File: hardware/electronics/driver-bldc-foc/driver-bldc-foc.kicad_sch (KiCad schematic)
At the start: 2 parts, among them U3 AP1117-33, U4 TPS563240

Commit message: fix pcb 20.7.1635
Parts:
- removed U4: TPS563240, symbol Custom:TPS563240
- added C10, C11, C6, C8: 100nF, Capacitor_SMD:C_0805_2012Metric, symbol JLCPCB-Capacitors:0805,10uF
- added C12, C5: 10uF, Capacitor_SMD:C_0805_2012Metric, symbol JLCPCB-Capacitors:0805,10uF
- added C7, C9: 1uF, Capacitor_SMD:C_0805_2012Metric, symbol JLCPCB-Capacitors:0805,10uF
- added D1, D2: PMEG4005CEJ, Diode_SMD:D_SOD-323F, symbol Diode:PMEG4005CEJ
- added J1: VBUS, Connector_Wire:SolderWirePad_1x01_SMD_5x10mm, symbol Connector_Generic:Conn_01x01
- added J2: GND, Connector_Wire:SolderWirePad_1x01_SMD_5x10mm, symbol Connector_Generic:Conn_01x01
- added J3: USB_A, Connector_USB:USB_B_OST_USB-B1HSxx_Horizontal, symbol Connector:USB_A
- added J4: Motor_Phase_A, Connector_Wire:SolderWirePad_1x01_SMD_5x10mm, symbol Connector_Generic:Conn_01x01
- added J5: Motor_Phase_B, Connector_Wire:SolderWirePad_1x01_SMD_5x10mm, symbol Connector_Generic:Conn_01x01
- added J6: Motor_Phase_C, Connector_Wire:SolderWirePad_1x01_SMD_5x10mm, symbol Connector_Generic:Conn_01x01
- added L3: 1.5uH, Inductor_SMD:L_APV_ANR5040, symbol Device:L_Ferrite_Small
- added R3, R5, R6: 3k, Resistor_SMD:R_0805_2012Metric, symbol Device:R_Small
- added R4: 22k, Resistor_SMD:R_0805_2012Metric, symbol Device:R_Small
- added U1: TPS563240DDC, Package_TO_SOT_SMD:SOT-23-6, symbol Regulator_Switching:TPS563240DDC
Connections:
- net GND: now reaches U3.1 (GND)
- net GND: now also C10.2, C12.2, C5.2, C6.2, C7.2, C8.2, C9.2, J2.1 (Pin_1), R3.2, R6.2, U1.1 (GND)
- net +3.3V: now reaches U3.2 (VO)
- net +3.3V: now also C7.1, C8.1
- net +5V: now reaches U3.3 (VI)
- net +5V: now also C5.1, C6.1, D1.1 (K), D2.1 (K)
- new net: R3.1, R4.1, U1.4 (VFB)
- new net: C11.2, L3.1, U1.2 (SW)
- new net: C11.1, U1.6 (VBST)
- new net +12V: C10.1, C9.1, U1.3 (VIN), U1.5 (EN)
- new net 5V_BUCK: D2.2 (A), L3.2, R4.2
- new net USB_VBUS: D1.2 (A)
- new net VBUS: J1.1 (Pin_1), R5.1
- new net VbusSense: C12.1, R5.2, R6.1
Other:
- moved on the sheet: U3

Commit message: update main schematic
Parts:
- C12: value 10uF -> 1nF
- R5: value 3k -> 100k
- R6: value 3k -> 3.9k
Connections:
- net ThreePhaseBridge and Power/PHASE_C: now reaches J6.1 (Pin_1)
- net ThreePhaseBridge and Power/PHASE_A: now reaches J4.1 (Pin_1)
- net ThreePhaseBridge and Power/PHASE_B: now reaches J5.1 (Pin_1)
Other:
- sheet MCU ports: added 3V3_IN, DRV_EN, DRV_MISO, DRV_MOSI, DRV_SCK, DVR_CS, GND_IN, IA, IB, IC, OC, PWM_A+, PWM_A-, PWM_B+, PWM_B-, PWM_C+, PWM_C-, USB_D+, USB_D-, VA, VB, VBUS_SENSE, VC; removed none
- sheet ThreePhaseBridge and Power ports: added 3V3_IN, CUR_A, CUR_B, CUR_C, EN, FAULT, GND, INHA, INHB, INHC, INLA, INLB, INLC, PHASE_A, PHASE_B, PHASE_C, SPI_CLK, SPI_CS, SPI_MISO, SPI_MOSI, VBUS, VSENS_A, VSENS_B, VSENS_C; removed none

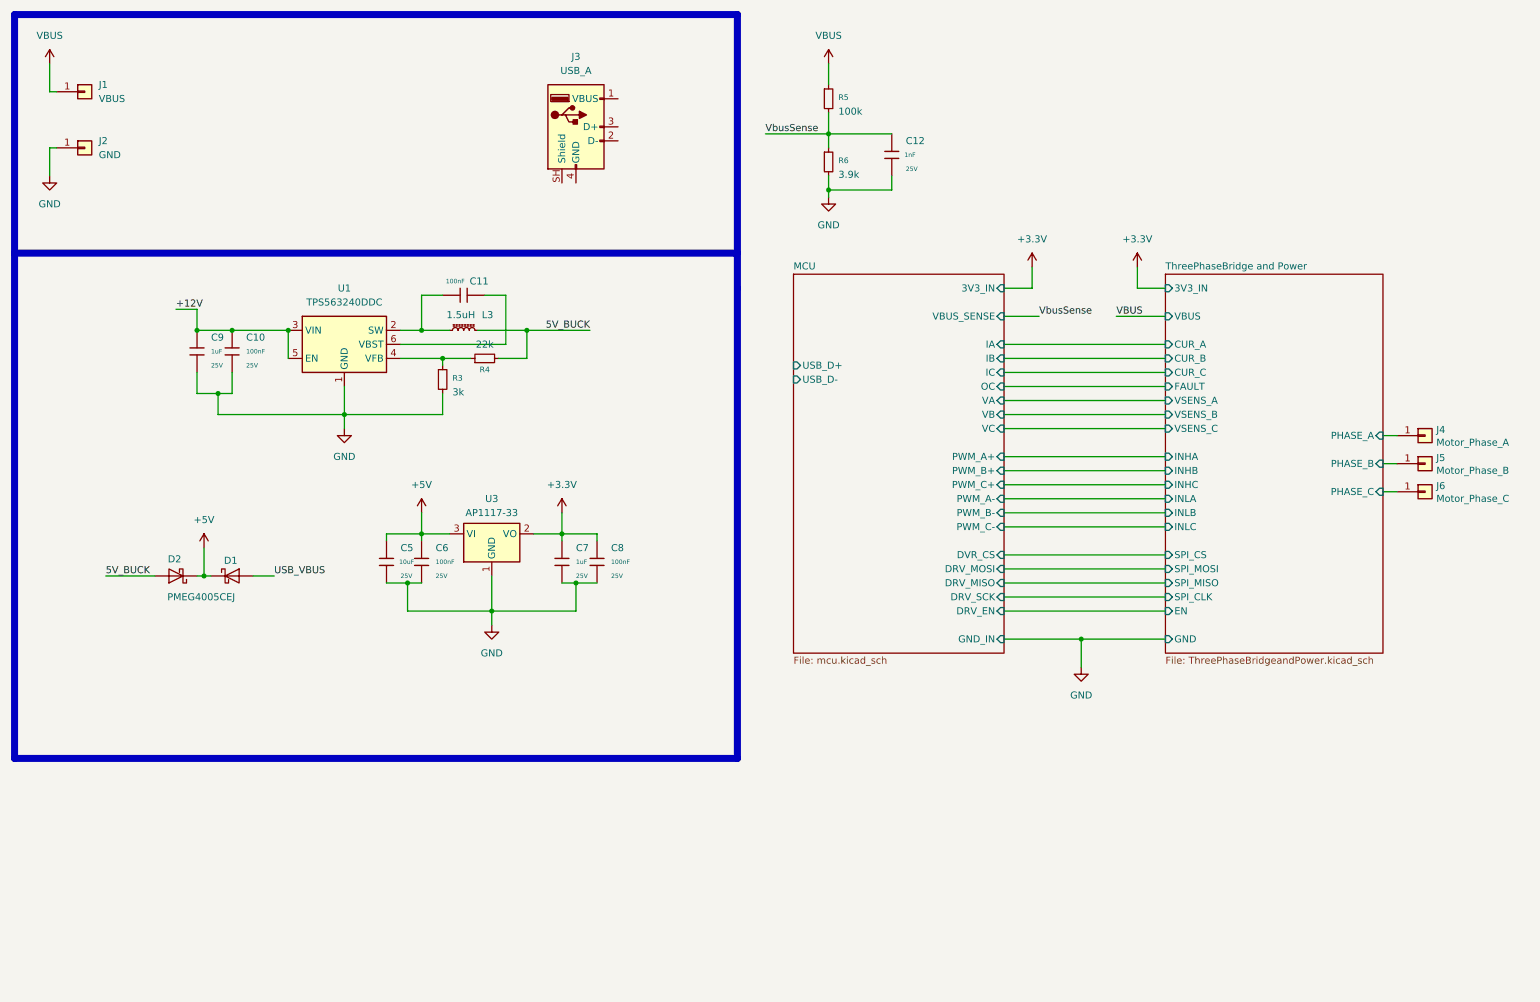
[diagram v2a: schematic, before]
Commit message: update top schematic
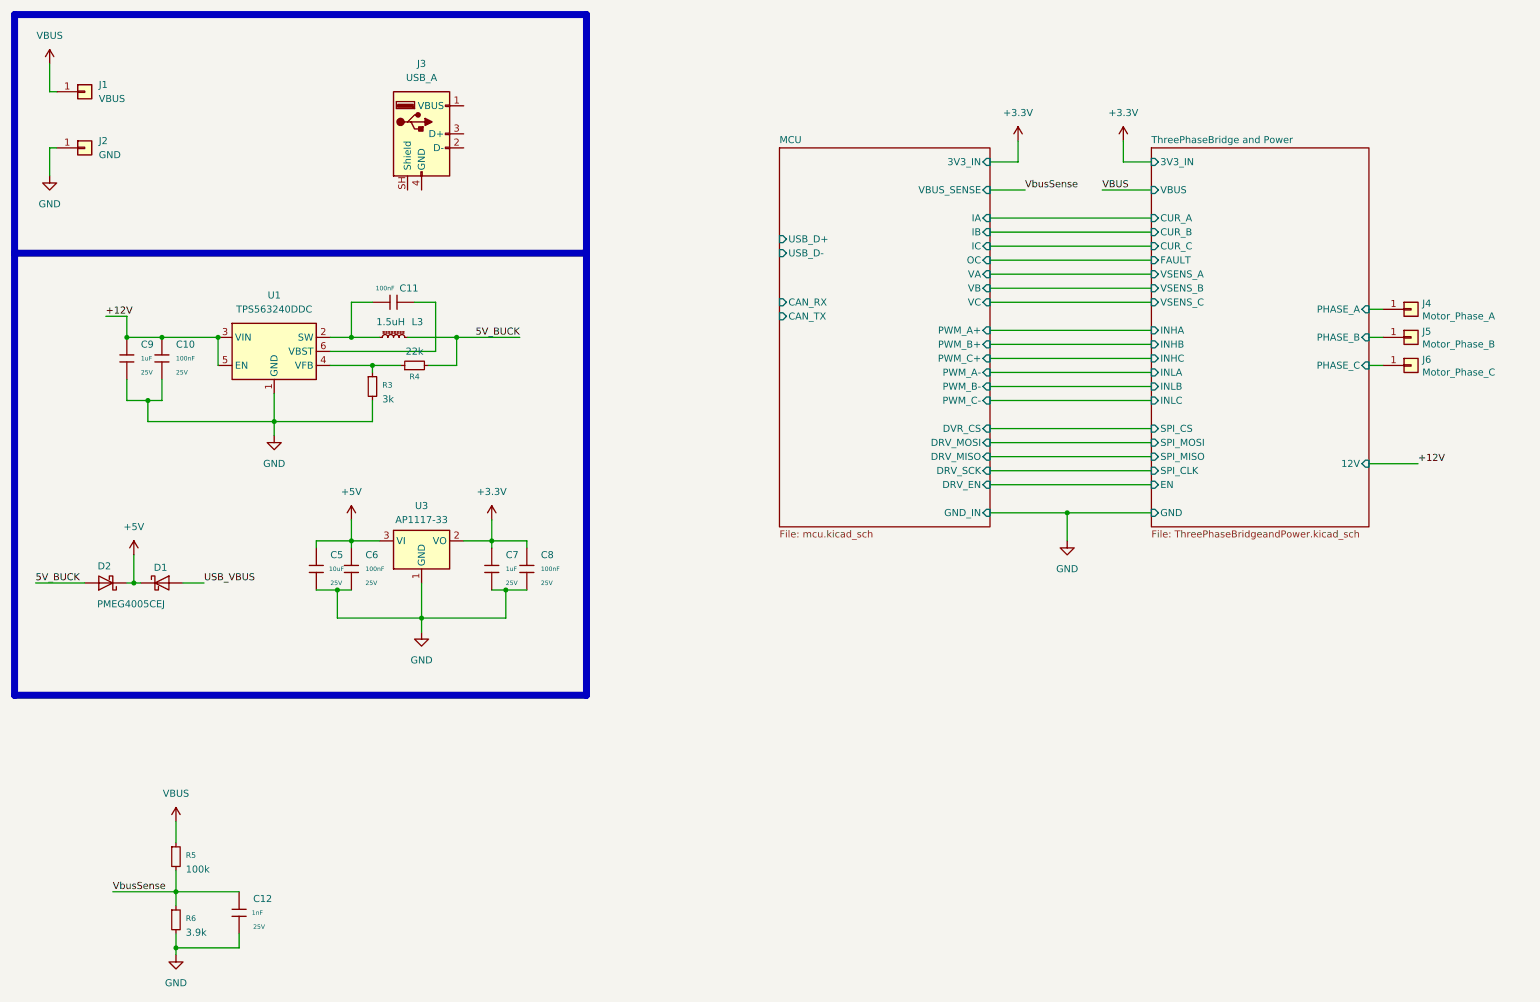
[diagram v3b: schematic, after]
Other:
- sheet MCU ports: added CAN_RX, CAN_TX; removed none
- sheet ThreePhaseBridge and Power ports: added 12V; removed none
- moved on the sheet: C10, C11, C12, C5, C6, C7, C8, C9, D1, D2, J3, J4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

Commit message: fix pcb
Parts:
- removed J1: VBUS, Connector_Wire:SolderWirePad_1x01_SMD_5x10mm, symbol Connector_Generic:Conn_01x01
- removed J2: GND, Connector_Wire:SolderWirePad_1x01_SMD_5x10mm, symbol Connector_Generic:Conn_01x01
- added J8: XT30PW-M, XT30PW-M:AMASS_XT30PW-M, symbol XT30PW-M:XT30PW-M
- added U5: TJA1051T-3, Package_SO:SOIC-8_3.9x4.9mm_P1.27mm, symbol Interface_CAN_LIN:TJA1051T-3
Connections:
- net +3.3V: now also U5.5 (VIO)
- net +5V: now also U5.3 (VCC)
- net GND: now also J3.4 (GND), J3.SH (Shield), J8.P, U5.2 (GND), U5.8 (S)
- net USB_VBUS: now also J3.1 (VBUS)
- net VBUS: now also J8.N
- net USB_D-: now reaches J3.2 (D-)
- net USB_D+: now reaches J3.3 (D+)
- new net CAN_RX: U5.4 (RXD)
- new net CAN_TX: U5.1 (TXD)
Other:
- sheet MCU ports: added DRV_CS, ENC_CS, ENC_EN, ENC_MISO, ENC_MOSI, ENC_SCK, ENC_SCL, ENC_SDA; removed DVR_CS
- moved on the sheet: J3

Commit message: update root schematic
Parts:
- removed J3: USB_A, Connector_USB:USB_B_OST_USB-B1HSxx_Horizontal, symbol Connector:USB_A
- removed J8: XT30PW-M, XT30PW-M:AMASS_XT30PW-M, symbol XT30PW-M:XT30PW-M
- added J1, J10, J11, J12, J13, J14, J15, J16, J17, J18, J19, J2, J20, J21, J22, J9: Conn_01x01_Pin, Connector_Wire:SolderWirePad_1x01_SMD_2x4mm, symbol Connector:Conn_01x01_Pin
- added J3: KH-TYPE-C-16P, KH-TYPE-C-16P:KINGHELM_KH-TYPE-C-16P, symbol KH-TYPE-C-16P:KH-TYPE-C-16P
- added R28, R29: 5.1k, Resistor_SMD:R_0805_2012Metric, symbol Device:R_Small
- added U6: XT30PW-M, XT30PW-M_AMA, symbol 2026-07-22_03-26-08:XT30PW-M
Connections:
- net USB_VBUS is gone; now on net VBUS: D1.2 (A)
- net +3.3V: now also J20.1 (Pin_1), J21.1 (Pin_1)
- net +5V: now also J22.1 (Pin_1)
- net GND: now also J17.1 (Pin_1), J18.1 (Pin_1), J19.1 (Pin_1), J3.A12B1 (GND), J3.A1B12 (GND), J3.SH1 (SHIELD), J3.SH2 (SHIELD), J3.SH3 (SHIELD), J3.SH4 (SHIELD), J9.1 (Pin_1), R28.1, R29.2, U6.1
- net MCU/ENC_CS: now also J16.1 (Pin_1)
- net MCU/ENC_EN: now also J15.1 (Pin_1)
- net MCU/ENC_MISO: now also J14.1 (Pin_1)
- net MCU/ENC_MOSI: now also J13.1 (Pin_1)
- net MCU/ENC_SCK: now also J12.1 (Pin_1)
- net MCU/ENC_SCL: now also J11.1 (Pin_1)
- net MCU/ENC_SDA: now also J10.1 (Pin_1)
- net USB_D+: now also J3.A6 (DP1), J3.B6 (DP2)
- net USB_D-: now also J3.A7 (DN1), J3.B7 (DN2)
- net VBUS: now also J3.A4B9 (VBUS), J3.A9B4 (VBUS), U6.2
- net at U5.6 (CANL): now also J2.1 (Pin_1)
- net at U5.7 (CANH): now also J1.1 (Pin_1)
- new net: J3.A5 (CC1), R28.2
- new net: J3.B5 (CC2), R29.1
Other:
- moved on the sheet: C10, C11, C12, C5, C6, C7, C8, C9, D1, D2, J4, J5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

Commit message: Update driver-bldc-foc schematics, PCB layout, and DRC reports
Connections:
- net VBUS: no longer D1.2 (A), J3.A4B9 (VBUS), J3.A9B4 (VBUS)
- new net V: D1.2 (A), J3.A4B9 (V), J3.A9B4 (V)
- no-connect marks 0 -> 2

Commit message: Complete PCB routing, fix net label connections, and export Gerber files for driver-bldc-foc
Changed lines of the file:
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@@
 	)
 	(junction
+		(at 83.82 27.94)
+		(diameter 0)
+		(color 0 0 0 0)
+	)
+	(junction
 		(at 35.56 74.93)
 		(diameter 0)
@@
 	(wire
 		(pts
-			(xy 81.28 27.94) (xy 87.63 27.94)
+			(xy 81.28 27.94) (xy 83.82 27.94)
 		)
 		(stroke
@@
 	(wire
 		(pts
+			(xy 83.82 25.4) (xy 83.82 27.94)
+		)
+		(stroke
+			(width 0)
+			(type default)
+		)
+	)
+	(wire
+		(pts
 			(xy 35.56 33.02) (xy 35.56 31.75)
 		)
@@
 	(wire
 		(pts
+			(xy 83.82 27.94) (xy 87.63 27.94)
+		)
+		(stroke
+			(width 0)
+			(type default)
+		)
+	)
+	(wire
+		(pts
 			(xy 152.4 170.18) (xy 152.4 172.72)
 		)
@@
 					(unit 1)
 				)
+			)
+		)
+	)
+	(symbol
+		(lib_id "power:PWR_FLAG")
+		(at 83.82 25.4 0)
+		(unit 1)
+		(body_style 1)
+		(exclude_from_sim no)
+		(in_bom yes)
+		(on_board yes)
+		(in_pos_files yes)
+		(dnp no)
+		(fields_autoplaced yes)
+		(property "Reference" "#FLG07"
+			(at 83.82 23.495 0)
+			(hide yes)
+			(show_name no)
+			(do_not_autoplace no)
+			(effects
+				(font
+					(size 1.27 1.27)
+				)
+			)
+		)
+		(property "Value" "PWR_FLAG"
+			(at 83.82 20.32 0)
+			(show_name no)
+			(do_not_autoplace no)
+			(effects
+				(font
+					(size 1.27 1.27)
+				)
+			)
+		)
+		(property "Footprint" ""
+			(at 83.82 25.4 0)
+			(hide yes)
+			(show_name no)
+			(do_not_autoplace no)
+			(effects
+				(font
+					(size 1.27 1.27)
+				)
+			)
+		)
+		(property "Datasheet" ""
+			(at 83.82 25.4 0)
+			(hide yes)
+			(show_name no)
+			(do_not_autoplace no)
+			(effects
+				(font
+					(size 1.27 1.27)
+				)
+			)
+		)
+		(property "Description" "Special symbol for telling ERC where power comes from"
+			(at 83.82 25.4 0)
+			(hide yes)
+			(show_name no)
+			(do_not_autoplace no)
+			(effects
+				(font
+					(size 1.27 1.27)
+				)
+			)
+		)
+		(pin "1"
+		)
+		(instances
+			(project "driver-bldc-foc"
+				(path "/90e88ac4-5a7b-4c35-8236-7462b7e2d3a9"
+					(reference "#FLG07")
+					(unit 1)
+				)
